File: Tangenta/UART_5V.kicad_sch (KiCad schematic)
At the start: 13 parts, among them J27 Conn_01x06_Pin, Q11 BSS138, Q12 BSS138, Q13 BSS138, Q14 BSS138

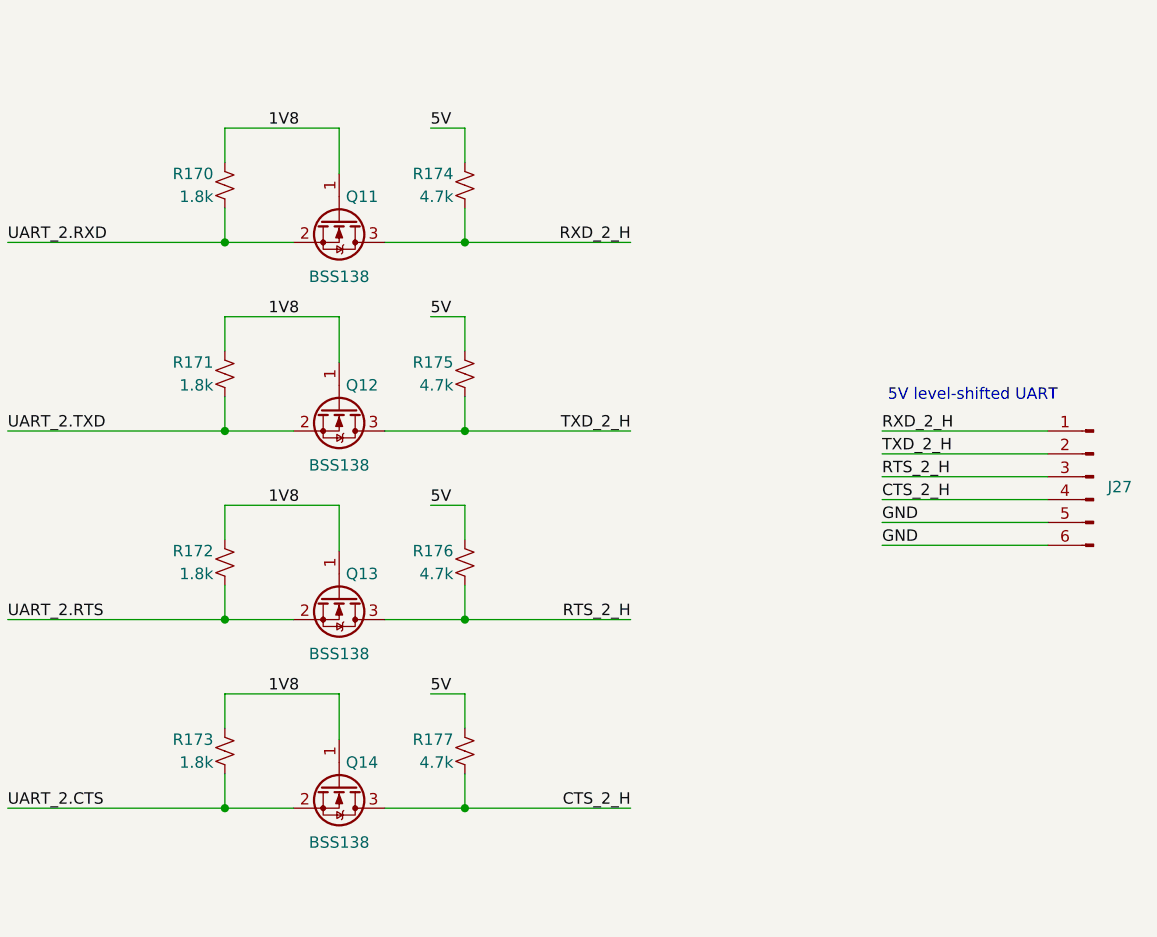
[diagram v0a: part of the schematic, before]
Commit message: Reverting to the original design.
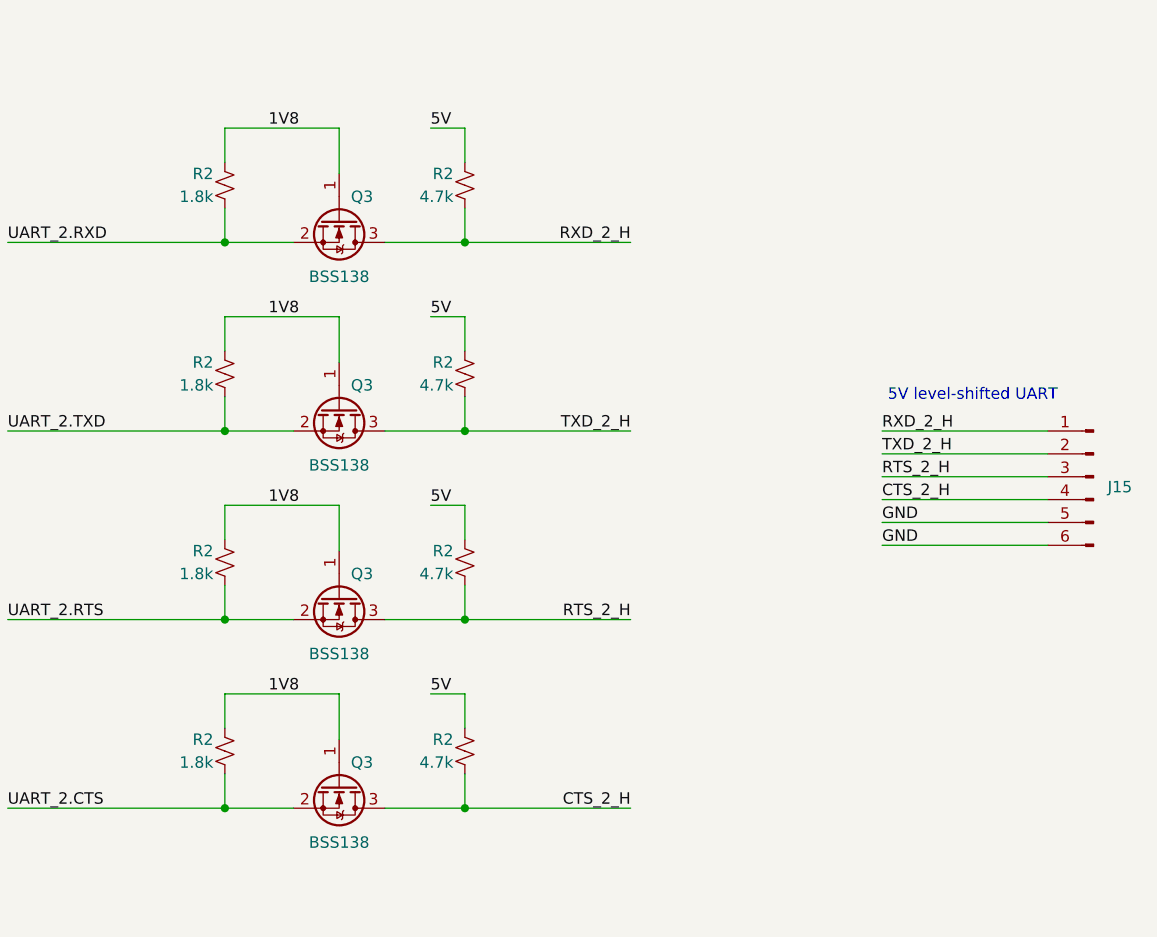
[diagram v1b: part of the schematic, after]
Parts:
- J15: renamed from J27; symbol Connector_Generic:Conn_01x06 -> CholaSymbolsPrjLib:Conn_01x06_Pin
- Q3: renamed from Q12; symbol Transistor_FET:BSS138 -> CholaSymbolsPrjLib:BSS138
- Q3: renamed from Q13; symbol Transistor_FET:BSS138 -> CholaSymbolsPrjLib:BSS138
- Q3: renamed from Q11; symbol Transistor_FET:BSS138 -> CholaSymbolsPrjLib:BSS138
- Q3: renamed from Q14; symbol Transistor_FET:BSS138 -> CholaSymbolsPrjLib:BSS138
- R2: renamed from R170; symbol Device:R_Small_US -> CholaSymbolsPrjLib:R_Small_US
- R2: renamed from R176; symbol Device:R_Small_US -> CholaSymbolsPrjLib:R_Small_US
- R2: renamed from R177; symbol Device:R_Small_US -> CholaSymbolsPrjLib:R_Small_US
- R2: renamed from R171; symbol Device:R_Small_US -> CholaSymbolsPrjLib:R_Small_US
- R2: renamed from R175; symbol Device:R_Small_US -> CholaSymbolsPrjLib:R_Small_US
- R2: renamed from R172; symbol Device:R_Small_US -> CholaSymbolsPrjLib:R_Small_US
- R2: renamed from R173; symbol Device:R_Small_US -> CholaSymbolsPrjLib:R_Small_US
- R2: renamed from R174; symbol Device:R_Small_US -> CholaSymbolsPrjLib:R_Small_US

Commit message: ...
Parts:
- J15: symbol CholaSymbolsPrjLib:Conn_01x06_Pin -> LocalPrjLib:Conn_01x06_Pin
- Q3: symbol CholaSymbolsPrjLib:BSS138 -> LocalPrjLib:BSS138
- R2: symbol CholaSymbolsPrjLib:R_Small_US -> LocalPrjLib:R_Small_US
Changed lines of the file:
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@@
     (effects (font (size 1.27 1.27)) (justify right))
   )
-  (symbol (lib_id "CholaSymbolsPrjLib:R_Small_US") (at 133.985 58.42 180) (unit 1)
+  (symbol (lib_id "LocalPrjLib:R_Small_US") (at 133.985 58.42 180) (unit 1)
     (in_bom yes) (on_board yes) (dnp no)
     (property "Reference" "R2" (at 132.715 57.15 0)
@@
     )
   )
-  (symbol (lib_id "CholaSymbolsPrjLib:R_Small_US") (at 160.655 100.33 180) (unit 1)
+  (symbol (lib_id "LocalPrjLib:R_Small_US") (at 160.655 100.33 180) (unit 1)
     (in_bom yes) (on_board yes) (dnp no)
     (property "Reference" "R2" (at 159.385 99.06 0)
@@
     )
   )
-  (symbol (lib_id "CholaSymbolsPrjLib:Conn_01x06_Pin") (at 230.505 90.805 0) (mirror y) (unit 1)
+  (symbol (lib_id "LocalPrjLib:Conn_01x06_Pin") (at 230.505 90.805 0) (mirror y) (unit 1)
     (in_bom yes) (on_board yes) (dnp no)
     (property "Reference" "J15" (at 233.426 91.948 0)
@@
     )
   )
-  (symbol (lib_id "CholaSymbolsPrjLib:BSS138") (at 146.685 83.185 270) (unit 1)
+  (symbol (lib_id "LocalPrjLib:BSS138") (at 146.685 83.185 270) (unit 1)
     (in_bom yes) (on_board yes) (dnp no)
     (property "Reference" "Q3" (at 149.225 80.645 90)
@@
     )
   )
-  (symbol (lib_id "CholaSymbolsPrjLib:BSS138") (at 146.685 104.14 270) (unit 1)
+  (symbol (lib_id "LocalPrjLib:BSS138") (at 146.685 104.14 270) (unit 1)
     (in_bom yes) (on_board yes) (dnp no)
     (property "Reference" "Q3" (at 149.225 101.6 90)
@@
     )
   )
-  (symbol (lib_id "CholaSymbolsPrjLib:R_Small_US") (at 160.655 121.285 180) (unit 1)
+  (symbol (lib_id "LocalPrjLib:R_Small_US") (at 160.655 121.285 180) (unit 1)
     (in_bom yes) (on_board yes) (dnp no)
     (property "Reference" "R2" (at 159.385 120.015 0)
@@
     )
   )
-  (symbol (lib_id "CholaSymbolsPrjLib:R_Small_US") (at 133.985 79.375 180) (unit 1)
+  (symbol (lib_id "LocalPrjLib:R_Small_US") (at 133.985 79.375 180) (unit 1)
     (in_bom yes) (on_board yes) (dnp no)
     (property "Reference" "R2" (at 132.715 78.105 0)
@@
     )
   )
-  (symbol (lib_id "CholaSymbolsPrjLib:R_Small_US") (at 160.655 79.375 180) (unit 1)
+  (symbol (lib_id "LocalPrjLib:R_Small_US") (at 160.655 79.375 180) (unit 1)
     (in_bom yes) (on_board yes) (dnp no)
     (property "Reference" "R2" (at 159.385 78.105 0)
@@
     )
   )
-  (symbol (lib_id "CholaSymbolsPrjLib:BSS138") (at 146.685 62.23 270) (unit 1)
+  (symbol (lib_id "LocalPrjLib:BSS138") (at 146.685 62.23 270) (unit 1)
     (in_bom yes) (on_board yes) (dnp no)
     (property "Reference" "Q3" (at 149.225 59.69 90)
@@
     )
   )
-  (symbol (lib_id "CholaSymbolsPrjLib:R_Small_US") (at 133.985 100.33 180) (unit 1)
+  (symbol (lib_id "LocalPrjLib:R_Small_US") (at 133.985 100.33 180) (unit 1)
     (in_bom yes) (on_board yes) (dnp no)
     (property "Reference" "R2" (at 132.715 99.06 0)
@@
     )
   )
-  (symbol (lib_id "CholaSymbolsPrjLib:BSS138") (at 146.685 125.095 270) (unit 1)
+  (symbol (lib_id "LocalPrjLib:BSS138") (at 146.685 125.095 270) (unit 1)
     (in_bom yes) (on_board yes) (dnp no)
     (property "Reference" "Q3" (at 149.225 122.555 90)
@@
     )
   )
-  (symbol (lib_id "CholaSymbolsPrjLib:R_Small_US") (at 133.985 121.285 180) (unit 1)
+  (symbol (lib_id "LocalPrjLib:R_Small_US") (at 133.985 121.285 180) (unit 1)
     (in_bom yes) (on_board yes) (dnp no)
     (property "Reference" "R2" (at 132.715 120.015 0)
@@
     )
   )
-  (symbol (lib_id "CholaSymbolsPrjLib:R_Small_US") (at 160.655 58.42 180) (unit 1)
+  (symbol (lib_id "LocalPrjLib:R_Small_US") (at 160.655 58.42 180) (unit 1)
     (in_bom yes) (on_board yes) (dnp no)
     (property "Reference" "R2" (at 159.385 57.15 0)

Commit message: Fixes, new approach.
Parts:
- J15: symbol LocalPrjLib:Conn_01x06_Pin -> LocalSymbolsPrjLib:Conn_01x06_Pin
- Q3: symbol LocalPrjLib:BSS138 -> LocalSymbolsPrjLib:BSS138
- R2: symbol LocalPrjLib:R_Small_US -> LocalSymbolsPrjLib:R_Small_US
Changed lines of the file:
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@@
     (effects (font (size 1.27 1.27)) (justify right))
   )
-  (symbol (lib_id "LocalPrjLib:R_Small_US") (at 133.985 58.42 180) (unit 1)
+  (symbol (lib_id "LocalSymbolsPrjLib:R_Small_US") (at 133.985 58.42 180) (unit 1)
     (in_bom yes) (on_board yes) (dnp no)
     (property "Reference" "R2" (at 132.715 57.15 0)
@@
     )
   )
-  (symbol (lib_id "LocalPrjLib:R_Small_US") (at 160.655 100.33 180) (unit 1)
+  (symbol (lib_id "LocalSymbolsPrjLib:R_Small_US") (at 160.655 100.33 180) (unit 1)
     (in_bom yes) (on_board yes) (dnp no)
     (property "Reference" "R2" (at 159.385 99.06 0)
@@
     )
   )
-  (symbol (lib_id "LocalPrjLib:Conn_01x06_Pin") (at 230.505 90.805 0) (mirror y) (unit 1)
+  (symbol (lib_id "LocalSymbolsPrjLib:Conn_01x06_Pin") (at 230.505 90.805 0) (mirror y) (unit 1)
     (in_bom yes) (on_board yes) (dnp no)
     (property "Reference" "J15" (at 233.426 91.948 0)
@@
     )
   )
-  (symbol (lib_id "LocalPrjLib:BSS138") (at 146.685 83.185 270) (unit 1)
+  (symbol (lib_id "LocalSymbolsPrjLib:BSS138") (at 146.685 83.185 270) (unit 1)
     (in_bom yes) (on_board yes) (dnp no)
     (property "Reference" "Q3" (at 149.225 80.645 90)
@@
     )
   )
-  (symbol (lib_id "LocalPrjLib:BSS138") (at 146.685 104.14 270) (unit 1)
+  (symbol (lib_id "LocalSymbolsPrjLib:BSS138") (at 146.685 104.14 270) (unit 1)
     (in_bom yes) (on_board yes) (dnp no)
     (property "Reference" "Q3" (at 149.225 101.6 90)
@@
     )
   )
-  (symbol (lib_id "LocalPrjLib:R_Small_US") (at 160.655 121.285 180) (unit 1)
+  (symbol (lib_id "LocalSymbolsPrjLib:R_Small_US") (at 160.655 121.285 180) (unit 1)
     (in_bom yes) (on_board yes) (dnp no)
     (property "Reference" "R2" (at 159.385 120.015 0)
@@
     )
   )
-  (symbol (lib_id "LocalPrjLib:R_Small_US") (at 133.985 79.375 180) (unit 1)
+  (symbol (lib_id "LocalSymbolsPrjLib:R_Small_US") (at 133.985 79.375 180) (unit 1)
     (in_bom yes) (on_board yes) (dnp no)
     (property "Reference" "R2" (at 132.715 78.105 0)
@@
     )
   )
-  (symbol (lib_id "LocalPrjLib:R_Small_US") (at 160.655 79.375 180) (unit 1)
+  (symbol (lib_id "LocalSymbolsPrjLib:R_Small_US") (at 160.655 79.375 180) (unit 1)
     (in_bom yes) (on_board yes) (dnp no)
     (property "Reference" "R2" (at 159.385 78.105 0)
@@
     )
   )
-  (symbol (lib_id "LocalPrjLib:BSS138") (at 146.685 62.23 270) (unit 1)
+  (symbol (lib_id "LocalSymbolsPrjLib:BSS138") (at 146.685 62.23 270) (unit 1)
     (in_bom yes) (on_board yes) (dnp no)
     (property "Reference" "Q3" (at 149.225 59.69 90)
@@
     )
   )
-  (symbol (lib_id "LocalPrjLib:R_Small_US") (at 133.985 100.33 180) (unit 1)
+  (symbol (lib_id "LocalSymbolsPrjLib:R_Small_US") (at 133.985 100.33 180) (unit 1)
     (in_bom yes) (on_board yes) (dnp no)
     (property "Reference" "R2" (at 132.715 99.06 0)
@@
     )
   )
-  (symbol (lib_id "LocalPrjLib:BSS138") (at 146.685 125.095 270) (unit 1)
+  (symbol (lib_id "LocalSymbolsPrjLib:BSS138") (at 146.685 125.095 270) (unit 1)
     (in_bom yes) (on_board yes) (dnp no)
     (property "Reference" "Q3" (at 149.225 122.555 90)
@@
     )
   )
-  (symbol (lib_id "LocalPrjLib:R_Small_US") (at 133.985 121.285 180) (unit 1)
+  (symbol (lib_id "LocalSymbolsPrjLib:R_Small_US") (at 133.985 121.285 180) (unit 1)
     (in_bom yes) (on_board yes) (dnp no)
     (property "Reference" "R2" (at 132.715 120.015 0)
@@
     )
   )
-  (symbol (lib_id "LocalPrjLib:R_Small_US") (at 160.655 58.42 180) (unit 1)
+  (symbol (lib_id "LocalSymbolsPrjLib:R_Small_US") (at 160.655 58.42 180) (unit 1)
     (in_bom yes) (on_board yes) (dnp no)
     (property "Reference" "R2" (at 159.385 57.15 0)

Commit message: Fixes...
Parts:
- renumbered J15 to J27, Q3 to Q11, Q3 to Q12, Q3 to Q13, Q3 to Q14, R2 to R170, R2 to R171, R2 to R172, R2 to R173, R2 to R174, R2 to R175, R2 to R176, R2 to R177
